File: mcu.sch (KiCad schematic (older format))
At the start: 28 parts

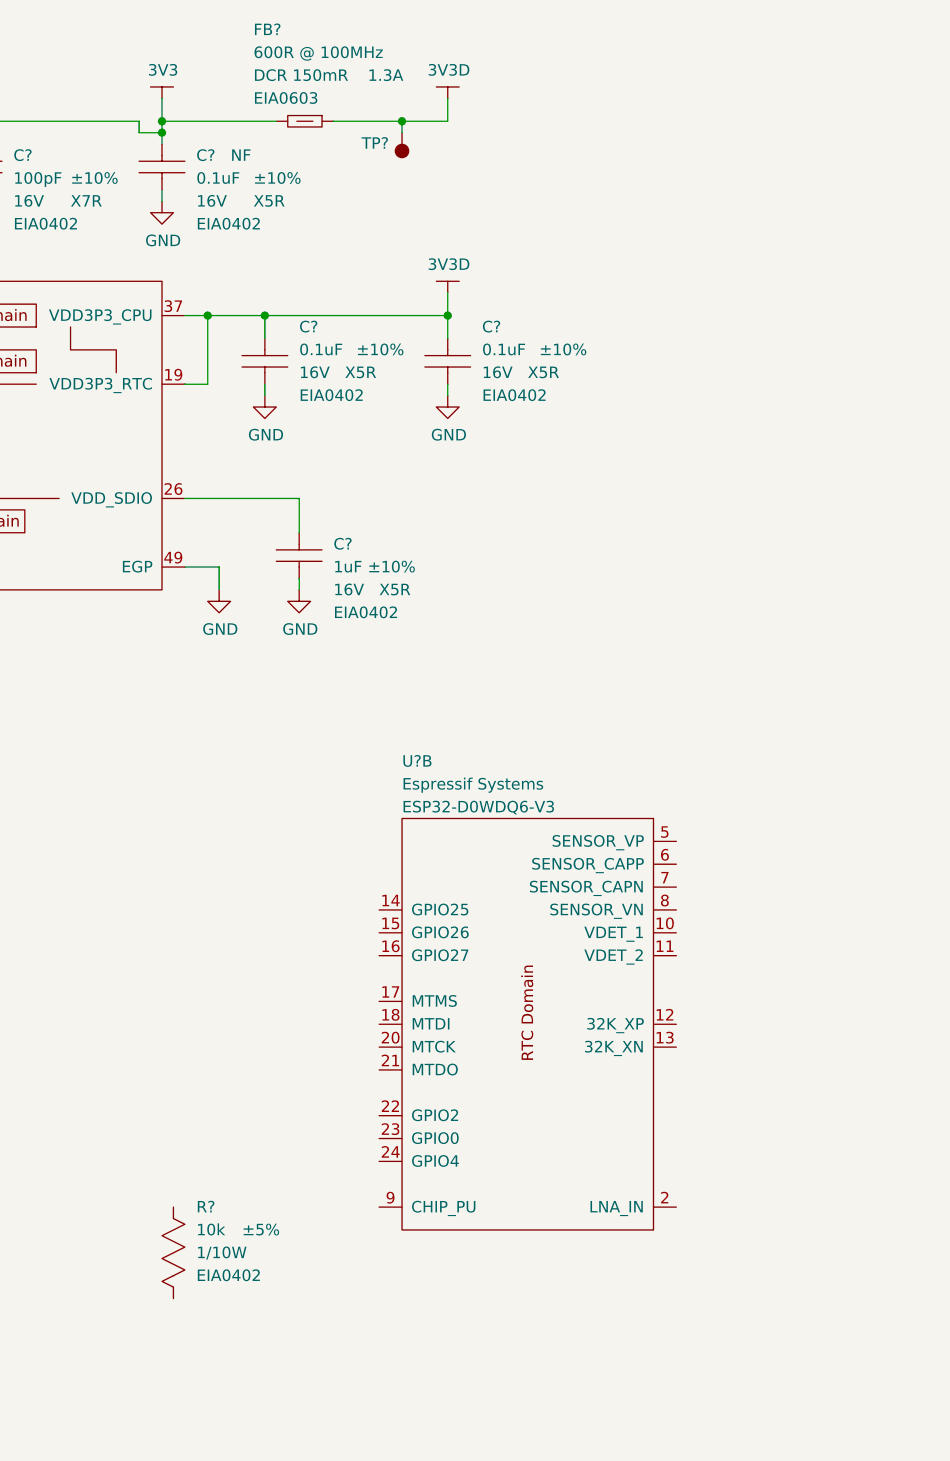
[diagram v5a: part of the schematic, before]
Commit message: Add ESP32 reset line C and label.
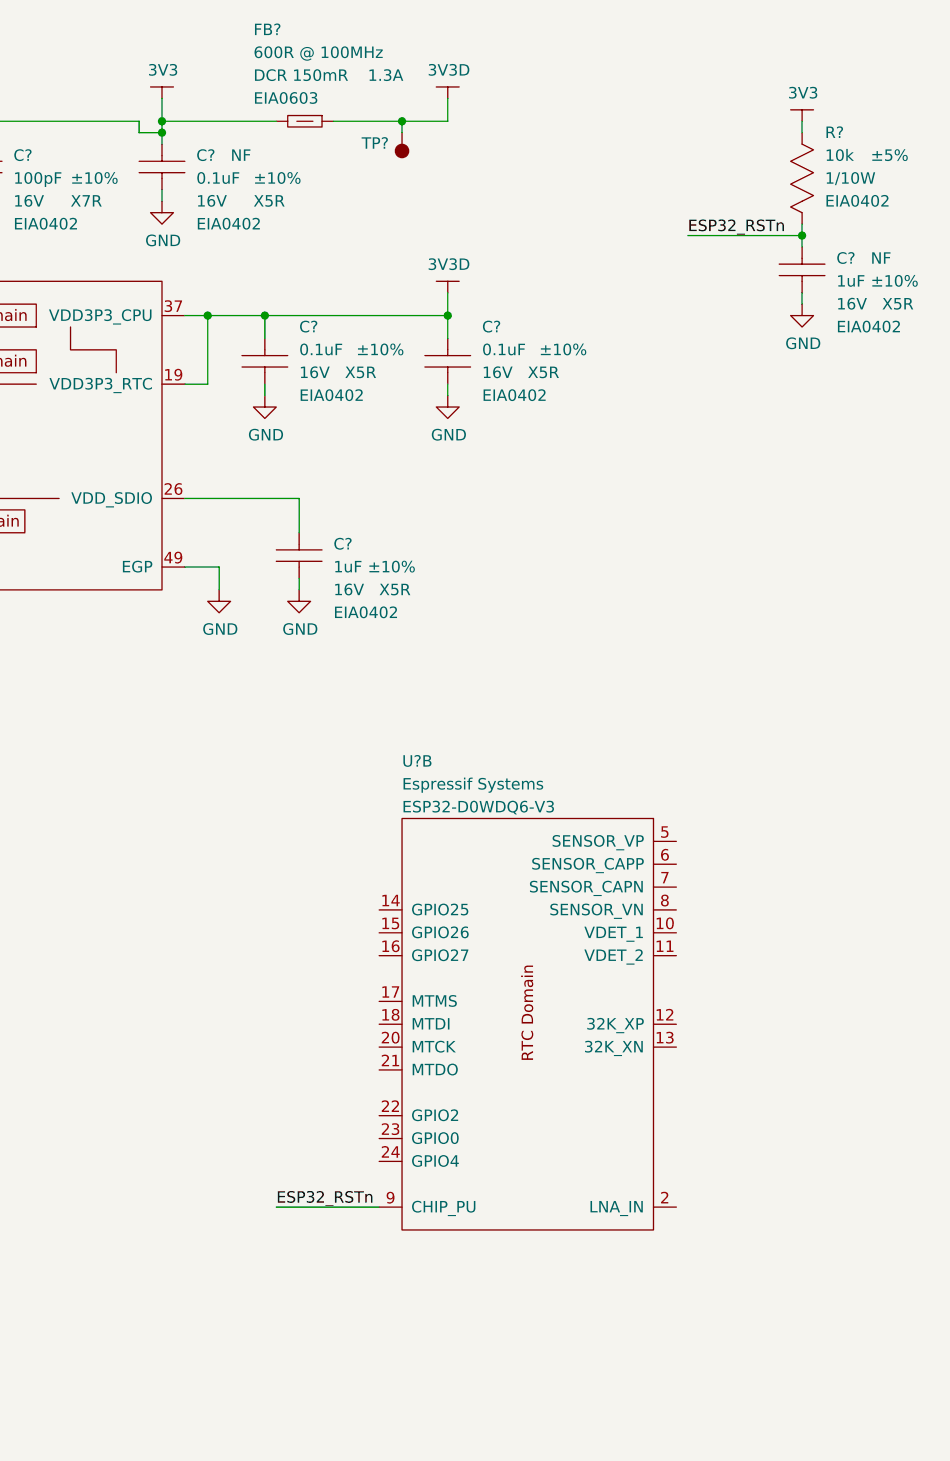
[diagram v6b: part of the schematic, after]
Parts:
- added C?: CAP-EIA0402, footprints_generic:CAPC100X50X55L30N, symbol gz_Ceramic-Capacitors:CAP-EIA0402
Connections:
- net +3V3: now also R?.1
- net GND: now also C?.2
- net ESP32_RSTn: now reaches U?.9 (CHIP_PU)
- net ESP32_RSTn: now also R?.2, C?.1
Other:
- moved on the sheet: R?
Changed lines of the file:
@@
 L gz_Chip-Resistors-Surface-Mount:RES-EIA0402 R?
 U 1 1 605F571C
-P 7250 6150
-F 0 "R?" V 7050 6250 50  0000 L CNN
-F 1 "RES-EIA0402" H 8050 7050 50  0001 L CNN
-F 2 "footprints_generic:RESC100X50X40L25NN" H 3950 10500 50  0001 L CNN
-F 3 "${PANASONIC_GP_CHIP_RES_BASE}ERJ2GEJ103X" H 3950 10600 50  0001 L CNN
-F 4 "Digikey" H 7250 6150 50  0001 L CNN "Vendor"
-F 5 "P10KJCT-ND" H 7250 6150 50  0001 L CNN "Vendor_PN"
-F 6 "Panasonic Electronic Components" H 8050 6850 50  0001 L CNN "Manufacturer"
-F 7 "ERJ2GEJ103X" H 8050 6750 50  0001 L CNN "MPN"
-F 8 "Resistors" H 3950 10900 50  0001 L CNN "Category"
-F 9 "Chip Resistor - Surface Mount" H 3950 11000 50  0001 L CNN "Family"
-F 10 "Yes" H 7250 6150 50  0001 C CNN "Fit"
-F 11 "10k" V 7150 6250 50  0000 L CNN "Resistance"
-F 12 "±5%" V 7150 6450 50  0000 L CNN "Tolerance"
-F 13 "1/10W" V 7250 6250 50  0000 L CNN "Power"
-F 14 "N/A" H 7250 6365 50  0001 L CNN "Voltage"
-F 15 "EIA0402" V 7350 6250 50  0000 L CNN "Package"
-	1    7250 6150
+P 10000 1450
+F 0 "R?" V 9800 1550 50  0000 L CNN
+F 1 "RES-EIA0402" H 10800 2350 50  0001 L CNN
+F 2 "footprints_generic:RESC100X50X40L25NN" H 6700 5800 50  0001 L CNN
+F 3 "${PANASONIC_GP_CHIP_RES_BASE}ERJ2GEJ103X" H 6700 5900 50  0001 L CNN
+F 4 "Digikey" H 10000 1450 50  0001 L CNN "Vendor"
+F 5 "P10KJCT-ND" H 10000 1450 50  0001 L CNN "Vendor_PN"
+F 6 "Panasonic Electronic Components" H 10800 2150 50  0001 L CNN "Manufacturer"
+F 7 "ERJ2GEJ103X" H 10800 2050 50  0001 L CNN "MPN"
+F 8 "Resistors" H 6700 6200 50  0001 L CNN "Category"
+F 9 "Chip Resistor - Surface Mount" H 6700 6300 50  0001 L CNN "Family"
+F 10 "Yes" H 10000 1450 50  0001 C CNN "Fit"
+F 11 "10k" V 9900 1550 50  0000 L CNN "Resistance"
+F 12 "±5%" V 9900 1750 50  0000 L CNN "Tolerance"
+F 13 "1/10W" V 10000 1550 50  0000 L CNN "Power"
+F 14 "N/A" H 10000 1665 50  0001 L CNN "Voltage"
+F 15 "EIA0402" V 10100 1550 50  0000 L CNN "Package"
+	1    10000 1450
 	0    1    1    0
 $EndComp
+$Comp
+L gz_Ceramic-Capacitors:CAP-EIA0402 C?
+U 1 1 605F9AA8
+P 10000 1850
+F 0 "C?" V 9950 2000 50  0000 L CNN
+F 1 "CAP-EIA0402" H 10400 2950 50  0001 L CNN
+F 2 "footprints_generic:CAPC100X50X55L30N" H 6700 6200 50  0001 L CNN
+F 3 "${KEMET_MLCC_BASE}C0402C105K4PACTU" H 6700 6300 50  0001 L CNN
+F 4 "Digikey" H 10000 1850 50  0001 L CNN "Vendor"
+F 5 "399-12289-1-ND" H 10000 1850 50  0001 L CNN "Vendor_PN"
+F 6 "KEMET" H 10400 2750 50  0001 L CNN "Manufacturer"
+F 7 "C0402C105K4PACTU" H 10400 2650 50  0001 L CNN "MPN"
+F 8 "Capacitors" H 6700 6600 50  0001 L CNN "Category"
+F 9 "Ceramic Capacitors" H 6700 6700 50  0001 L CNN "Family"
+F 10 "NF" V 9950 2150 50  0000 L CNN "Fit"
+F 11 "1uF" V 10050 2000 50  0000 L CNN "Capacitance"
+F 12 "±10%" V 10050 2150 50  0000 L CNN "Tolerance"
+F 13 "16V" V 10150 2000 50  0000 L CNN "Voltage"
+F 14 "X5R" V 10150 2200 50  0000 L CNN "Dielectric"
+F 15 "EIA0402" V 10250 2000 50  0000 L CNN "Package"
+	1    10000 1850
+	0    1    1    0
+$EndComp
+$Comp
+L gz_Power-Symbols:GND #PWR?
+U 1 1 60607E38
+P 10000 2000
+F 0 "#PWR?" H 10000 1750 50  0001 C CNN
+F 1 "GND" H 10005 1827 50  0000 C CNN
+F 2 "" H 10000 2000 50  0001 C CNN
+F 3 "" H 10000 2000 50  0001 C CNN
+	1    10000 2000
+	1    0    0    -1
+$EndComp
+$Comp
+L gz_Power-Symbols:3V3 #PWR?
+U 1 1 606086F3
+P 10000 1200
+F 0 "#PWR?" H 10150 1150 50  0001 C CNN
+F 1 "3V3" H 10005 1323 50  0000 C CNN
+F 2 "" H 10000 1200 50  0001 C CNN
+F 3 "" H 10000 1200 50  0001 C CNN
+	1    10000 1200
+	1    0    0    -1
+$EndComp
+Wire Wire Line
+	10000 1200 10000 1250
+Wire Wire Line
+	10000 1650 10000 1700
+Wire Wire Line
+	10000 1950 10000 2000
+Wire Wire Line
+	10000 1700 9500 1700
+Connection ~ 10000 1700
+Wire Wire Line
+	10000 1700 10000 1750
+Text Label 9500 1700 0    50   ~ 0
+ESP32_RSTn
+Wire Wire Line
+	8150 5950 7700 5950
+Text Label 7700 5950 0    50   ~ 0
+ESP32_RSTn
 $EndSCHEMATC
